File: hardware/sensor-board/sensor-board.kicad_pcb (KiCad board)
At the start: 2 copper layers, 65 x 56 mm, 55 parts, among them J1 HELM, J2 TACH, J3 PROBES, J4 RPi GPIO, U1 ADS1115IDGSR, U2 ADS1115IDGSR, U3 PC817

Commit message: Sensor board rev 1.1: isolated NMEA 2000 on the board
The Fusion stereo (and the depth transducer) now reach the Pi through the
sensor board itself, not a separate CAN HAT:

- MCP2518FD CAN FD controller on SPI0 (GPIO 8-11), interrupt on GPIO 25,
  40 MHz oscillator: Raspberry Pi OS's mcp251xfd overlay makes it can0
- ISO1044 isolated transceiver; the network side is powered from NET-S
  through reverse-polarity, surge and ESD protection and a 5 V regulator,
  referenced to the network's own ground (about 1 LEN)
- J5, a 5-pin locking plug for a drop cable, Micro-C pin order; a 120 ohm
  bench-only terminator behind an open solder jumper
- the network side is its own island: 2 mm from all other copper (DRC rule),
  its own ground pour, kept clear of the Pi mounting hole beside it

The board grows from 65 x 56 to 65 x 76 mm on the side away from the header
(the tach moves down with it, both field plugs on the bottom edge), with a
fifth mounting hole. ERC, DRC and schematic parity all clean.

Also fixes the schematic generator: two symbols derived from one library
parent (SMAJ5.0A, SMAJ18A) shared their unit lists, so renaming one renamed
both and KiCad refused the file; and custom-shaped pads (SOT-89 tab, solder
jumper) are now routed around by their true outline.

Co-Authored-By: Claude Opus 5.5 <noreply@anthropic.com>
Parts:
- added C12: 100n, sensor-board:C_0805_2012Metric_NoSilk, F.Cu at (113.0, 92.2)
- added C13: 1u, sensor-board:C_0805_2012Metric_NoSilk, F.Cu at (113.0, 95.6)
- added C14: 100n, sensor-board:C_0805_2012Metric_NoSilk, F.Cu at (128.5, 92.0)
- added C15: 100n, sensor-board:C_0805_2012Metric_NoSilk, F.Cu at (122.0, 99.8)
- added C16: 1u, sensor-board:C_1206_3216Metric_NoSilk, F.Cu at (117.8, 109.0)
- added C17: 1u, sensor-board:C_0805_2012Metric_NoSilk, F.Cu at (120.3, 109.0)
- added C18: 100n, sensor-board:C_0805_2012Metric_NoSilk, F.Cu at (121.6, 105.2)
- added D10: SMAJ18A, Diode_SMD:D_SMA, F.Cu at (105.5, 112.0)
- added D11: NUP2105L, sensor-board:SOT-23_NoSilk, F.Cu at (125.0, 111.5)
- added D9: SS14, Diode_SMD:D_SMA, F.Cu at (105.5, 108.2)
- added H5: MountingHole, MountingHole:MountingHole_2.7mm_M2.5, F.Cu at (161.5, 122.5)
- added J5: NMEA 2000, Connector_Phoenix_MC:PhoenixContact_MC_1,5_5-GF-3.81_1x05_P3.81mm_Horizontal_ThreadedFlange, F.Cu at (109.0, 117.3)
- added JP1: TERM, Jumper:SolderJumper-2_P1.3mm_Open_RoundedPad1.0x1.5mm, F.Cu at (128.5, 111.8)
- added R26: 120, sensor-board:R_0805_2012Metric_NoSilk, F.Cu at (128.5, 108.0)
- added R27: 10k, sensor-board:R_0805_2012Metric_NoSilk, F.Cu at (132.2, 92.0)
- added R28: 10k, sensor-board:R_0805_2012Metric_NoSilk, F.Cu at (132.2, 96.0)
- added U4: MCP2518FD, Package_SO:SOIC-14_3.9x8.7mm_P1.27mm, F.Cu at (120.5, 94.3)
- added U5: ISO1044BD, Package_SO:SOIC-8_3.9x4.9mm_P1.27mm, F.Cu at (116.5, 102.0)
- added U6: L78L05, Package_TO_SOT_SMD:SOT-89-3, F.Cu at (113.5, 109.0)
- added Y1: 40MHz, Oscillator:Oscillator_SMD_Abracon_ASE-4Pin_3.2x2.5mm, F.Cu at (128.5, 95.5)
- moved C11 20.0 mm to (147.3, 111.5)
- moved D7 20.0 mm to (144.4, 111.5)
- moved J2 20.0 mm to (142.0, 117.3)
- moved R19 20.0 mm to (136.0, 111.5)
- moved R20 20.0 mm to (138.8, 111.5)
- moved R21 20.0 mm to (141.6, 111.5)
- moved U3 20.0 mm to (155.5, 111.5)
- moved R23 18.5 mm to (155.5, 104.3)
- moved R22 16.6 mm to (155.5, 101.8)
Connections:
- J4 pad 19: unconnected-(J4-Pin_19-Pad19) -> /SPI_MOSI
- J4 pad 21: unconnected-(J4-Pin_21-Pad21) -> /SPI_MISO
- J4 pad 22: unconnected-(J4-Pin_22-Pad22) -> /CAN_INT
- J4 pad 23: unconnected-(J4-Pin_23-Pad23) -> /SPI_SCLK
- J4 pad 24: unconnected-(J4-Pin_24-Pad24) -> /SPI_CE0
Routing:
- net +3V3: track 109.6 -> 178.2 mm
- net /CAN_INT: track 0.00 -> 55.5 mm, vias 0 -> 2
- net /SPI_CE0: track 0.00 -> 54.4 mm, vias 0 -> 3
- net /SPI_MISO: track 0.00 -> 42.9 mm, vias 0 -> 2
- net /SPI_SCLK: track 0.00 -> 42.8 mm, vias 0 -> 4
- net /SPI_MOSI: track 0.00 -> 39.6 mm, vias 0 -> 1
- net /N2K_H: track 0.00 -> 26.7 mm, vias 0 -> 2
- net /N2K_GND: track 0.00 -> 23.1 mm, vias 0 -> 2
- net /N2K_L: track 0.00 -> 19.7 mm, vias 0 -> 7
- net /TACH_GPIO: track 33.1 -> 51.0 mm, vias 2 -> 0
- net /N2K_12V: track 0.00 -> 15.7 mm
- net /N2K_5V: track 0.00 -> 12.1 mm, vias 0 -> 4
- net /N2K_NET_S: track 0.00 -> 8.20 mm
- net /CAN_CLK: track 0.00 -> 6.98 mm
- net /N2K_TERM: track 0.00 -> 5.06 mm
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- added copper zone on B.Cu, net /N2K_GND
- added copper zone on F.Cu, net /N2K_GND
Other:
- board size 65 x 56 mm -> 65 x 76 mm
- board text added: "1 SHLD 2 NET-S 3 NET-C"
- board text added: "4 NET-H 5 NET-L"
- board text added: "Boat MFD sensor board r1.1"
- board text added: "J5 NMEA 2000 - ISOLATED"
- board text added: "TERM"
- board text removed: "Boat MFD sensor board r1.0"

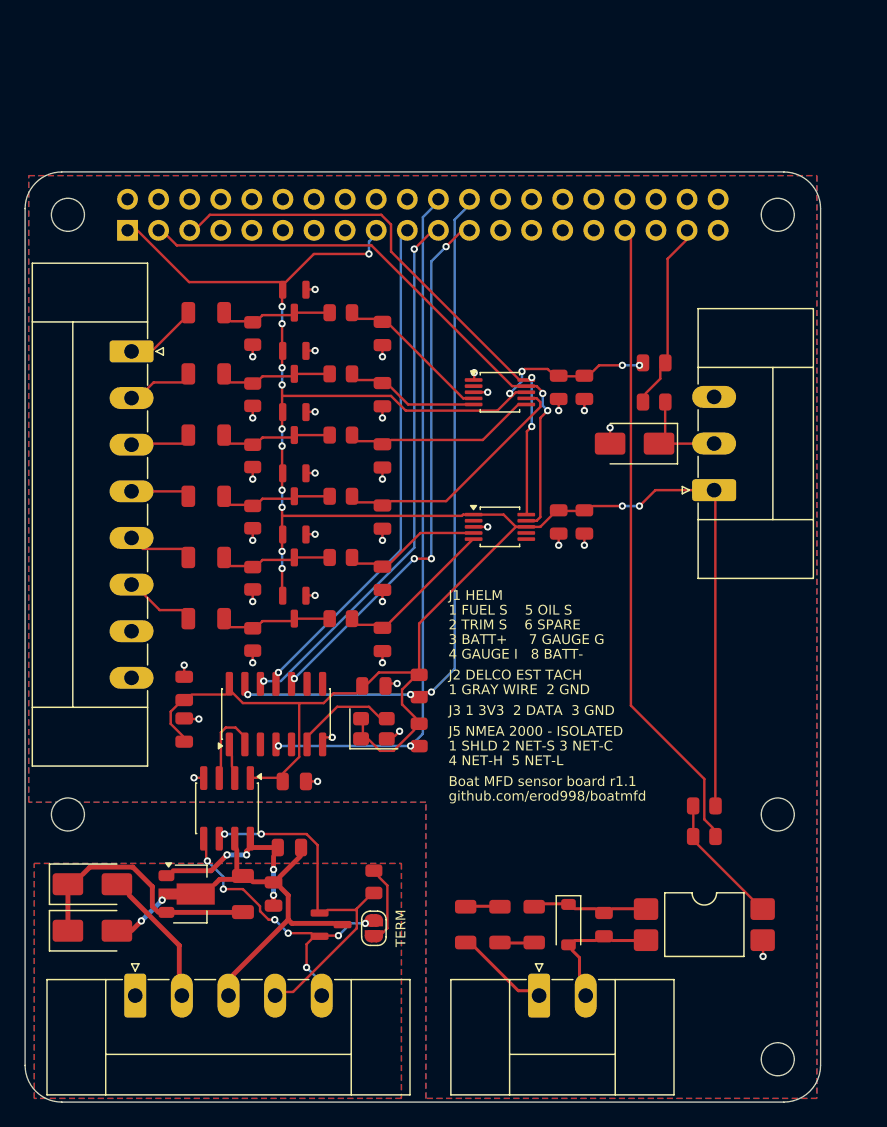
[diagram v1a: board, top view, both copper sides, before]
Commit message: Sensor board: pre-order review and PCBWay order package
Checked against the manufacturers' datasheets rather than KiCad's library:
ISO1044 (TI), MCP2518FD (Microchip Table 1-1), uA78L05 SOT-89 (TI),
NUP2105L (onsemi), EL817 incl. its SMD land pattern (Everlight), Abracon ASE.

Changes from the review:
- U6 is now TI's UA78L05ACPK, whose SOT-89 pinout (1 out, 2 gnd, 3 in) was
  read from TI's datasheet; ST's could not be retrieved to confirm
- C17 1 uF -> 4.7 uF: TI asks for ~4.7 uF bulk at the ISO1044's VCC2
- orderable part numbers for U3 (EL817S1(C)(TU)-F), Y1
  (ASE-40.000MHZ-L-C-T) and every Phoenix header and plug
- vias 0.6 -> 0.7 mm (0.2 mm ring; 0.15 was exactly PCBWay's minimum)
- silkscreen stroke 0.12 -> 0.15 mm (PCBWay's minimum)
- PCBWay's limits written into the design rules so DRC enforces them

fab/pcbway/: Gerbers, BOM and centroid in PCBWay's assembly format, and
ORDER.md with every option for the PCB and assembly quote forms.

Co-Authored-By: Claude Opus 5.5 <noreply@anthropic.com>
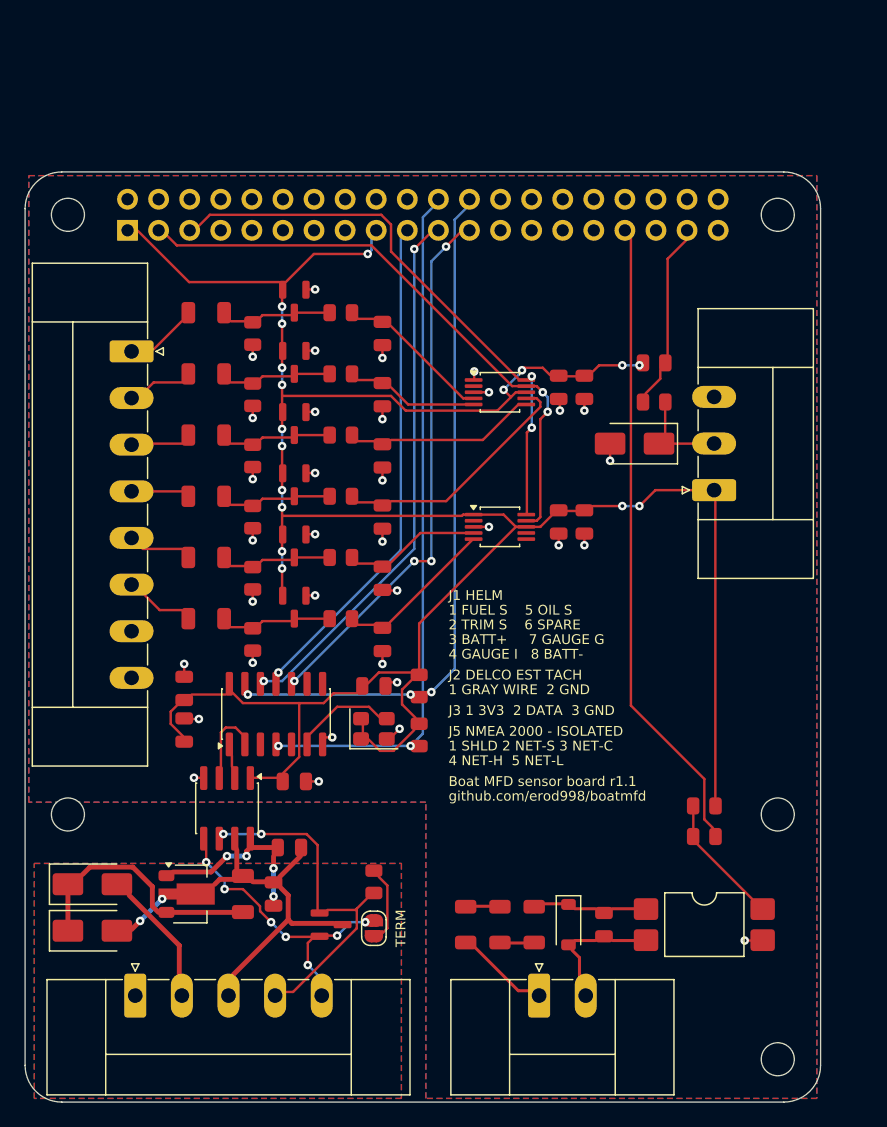
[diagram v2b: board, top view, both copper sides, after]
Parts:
- C17: value 1u -> 4.7u
- U3: value PC817 -> EL817
- U6: value L78L05 -> UA78L05
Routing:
- net GND: track 17.1 -> 18.2 mm
- net +3V3: track 178.2 -> 178.9 mm

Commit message: Sensor board rev 1.2: every connector pin labelled on the board
Each pin of J1, J2, J3 and J5 now has its connection printed beside it, on
the wire side of the connector: FUEL TRIM BAT+ IGN OIL SPARE GND GND on the
helm connector, TACH/GND on the tach, 3V3/DATA/GND on the probes, and the
NMEA 2000 drop cable's wire colours on J5. The numbered pinout block in the
middle is replaced by a WIRING block that says where each kind of wire goes.

Tach wording is for the newer EST coil only (BAT in, TACH out). The input
itself is unchanged: the coil's TACH terminal is its switched side and
spikes to a few hundred volts, which is what the optocoupler input is for.

Parts moved to make room for the labels; the pour is filled after the
board's connectivity is rebuilt, so slivers between the NMEA 2000 pads are
removed instead of left as floating copper. ERC, DRC and parity: clean.

Co-Authored-By: Claude Opus 5.5 <noreply@anthropic.com>
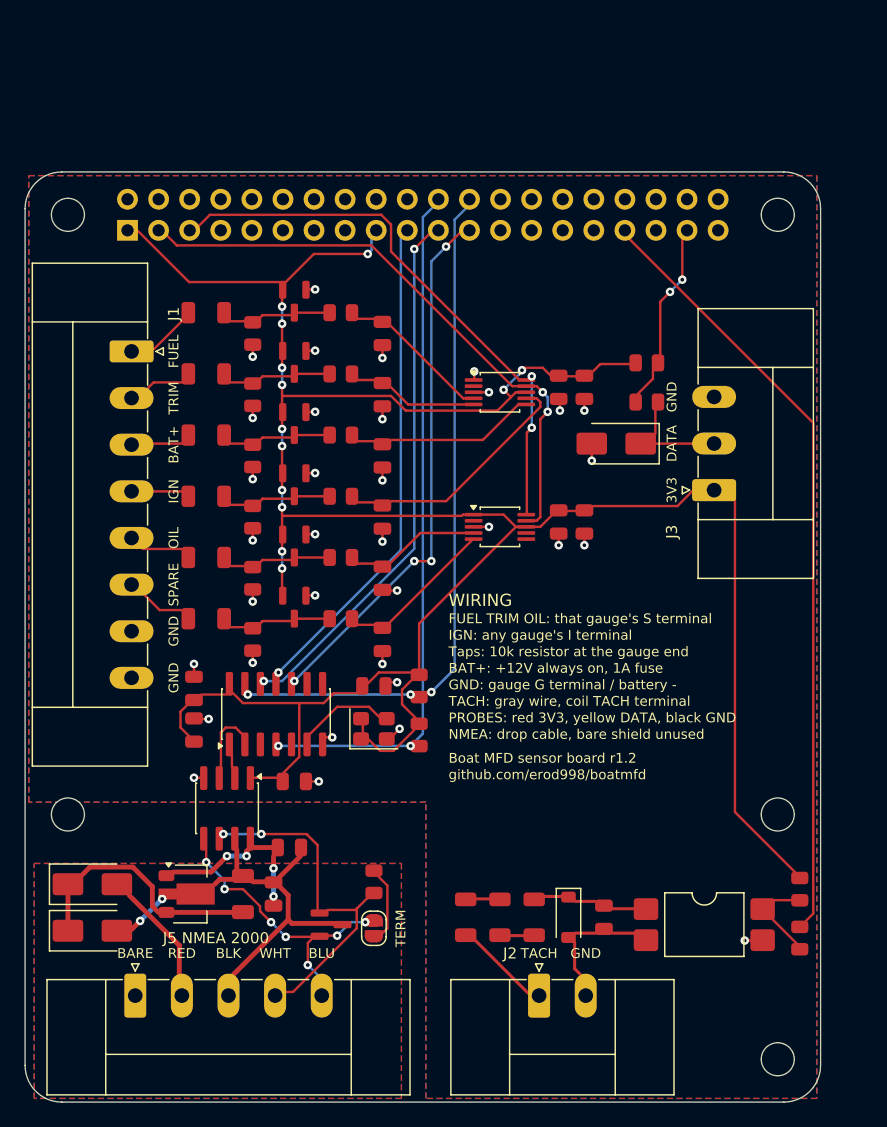
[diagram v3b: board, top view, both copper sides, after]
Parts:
- moved R23 11.4 mm to (163.3, 112.6), turned to 90 degrees
- moved R22 10.3 mm to (163.3, 108.6), turned to 90 degrees
- moved D8 1.50 mm to (148.3, 72.2)
- moved C12 0.80 mm to (113.8, 92.2)
- moved C13 0.80 mm to (113.8, 95.6)
- moved C11 0.60 mm to (147.3, 110.9)
- moved D7 0.60 mm to (144.4, 110.9)
- moved R19 0.60 mm to (136.0, 110.9)
- moved R20 0.60 mm to (138.8, 110.9)
- moved R21 0.60 mm to (141.6, 110.9)
- moved R24 0.60 mm to (150.8, 65.6)
- moved R25 0.60 mm to (150.8, 68.8)
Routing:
- net /TACH_GPIO: track 51.0 -> 62.2 mm
- net +3V3: track 178.9 -> 185.3 mm, vias 17 -> 13
- net /TACH_OUT: track 7.56 -> 4.33 mm
- net /OW_EXT: track 3.60 -> 5.10 mm
- net /TACH_GND: track 5.85 -> 6.41 mm
- net /OW: track 12.3 -> 12.5 mm, vias 0 -> 2
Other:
- board text added: "3V3"
- board text added: "BARE"
- board text added: "BAT+"
- board text added: "BAT+: +12V always on, 1A fuse"
- board text added: "BLK"
- board text added: "BLU"
- board text added: "Boat MFD sensor board r1.2"
- board text added: "DATA"
- board text added: "FUEL"
- board text added: "FUEL TRIM OIL: that gauge's S terminal"
- board text added: "GND"
- board text added: "GND: gauge G terminal / battery -"
- board text added: "IGN"
- board text added: "IGN: any gauge's I terminal"
- board text added: "J1"
- board text added: "J2"
- board text added: "J3"
- board text added: "J5 NMEA 2000"
- board text added: "NMEA: drop cable, bare shield unused"
- board text added: "OIL"
- board text added: "PROBES: red 3V3, yellow DATA, black GND"
- board text added: "RED"
- board text added: "SPARE"
- board text added: "TACH"
- board text added: "TACH: gray wire, coil TACH terminal"
- board text added: "TRIM"
- board text added: "Taps: 10k resistor at the gauge end"
- board text added: "WHT"
- board text added: "WIRING"
- board text removed: "1 FUEL S 5 OIL S"
- board text removed: "1 GRAY WIRE 2 GND"
- board text removed: "1 SHLD 2 NET-S 3 NET-C"
- board text removed: "2 TRIM S 6 SPARE"
- board text removed: "3 BATT+ 7 GAUGE G"
- board text removed: "4 GAUGE I 8 BATT-"
- board text removed: "4 NET-H 5 NET-L"
- board text removed: "Boat MFD sensor board r1.1"
- board text removed: "J1 HELM"
- board text removed: "J2 DELCO EST TACH"
- board text removed: "J3 1 3V3 2 DATA 3 GND"
- board text removed: "J5 NMEA 2000 - ISOLATED"

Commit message: Sensor board: J6 LIGHTS connector for a separate LED board
The LED controllers stay off this board (strip current next to the gauge
taps, and a shorted strip taking the engine data down with it). J6 gives
a future LED board what it needs from the Pi and nothing it switches:
3V3 for its logic, the I2C bus for PCA9685 PWM channels (as many as
needed), GPIO18 and GPIO19 (PWM0/PWM1) for two addressable strips, GPIO21
spare, and two grounds. JST GH 8-way, latching, SMD on the right edge
between the probe connector and the mounting hole; pins labelled on the
silkscreen.

The two lines from the header's far corner route on the bottom layer so
they don't wall off the header's GND pin 39 from the top pour. J6's GND
vias go in before routing. BOM marks J6 SMD (only the Phoenix blocks and
the header are through-hole). SENSOR_BOARD.md documents the interface and
the rules for the LED board; README points to it.

ERC, DRC and parity: clean.

Co-Authored-By: Claude Opus 5.5 <noreply@anthropic.com>
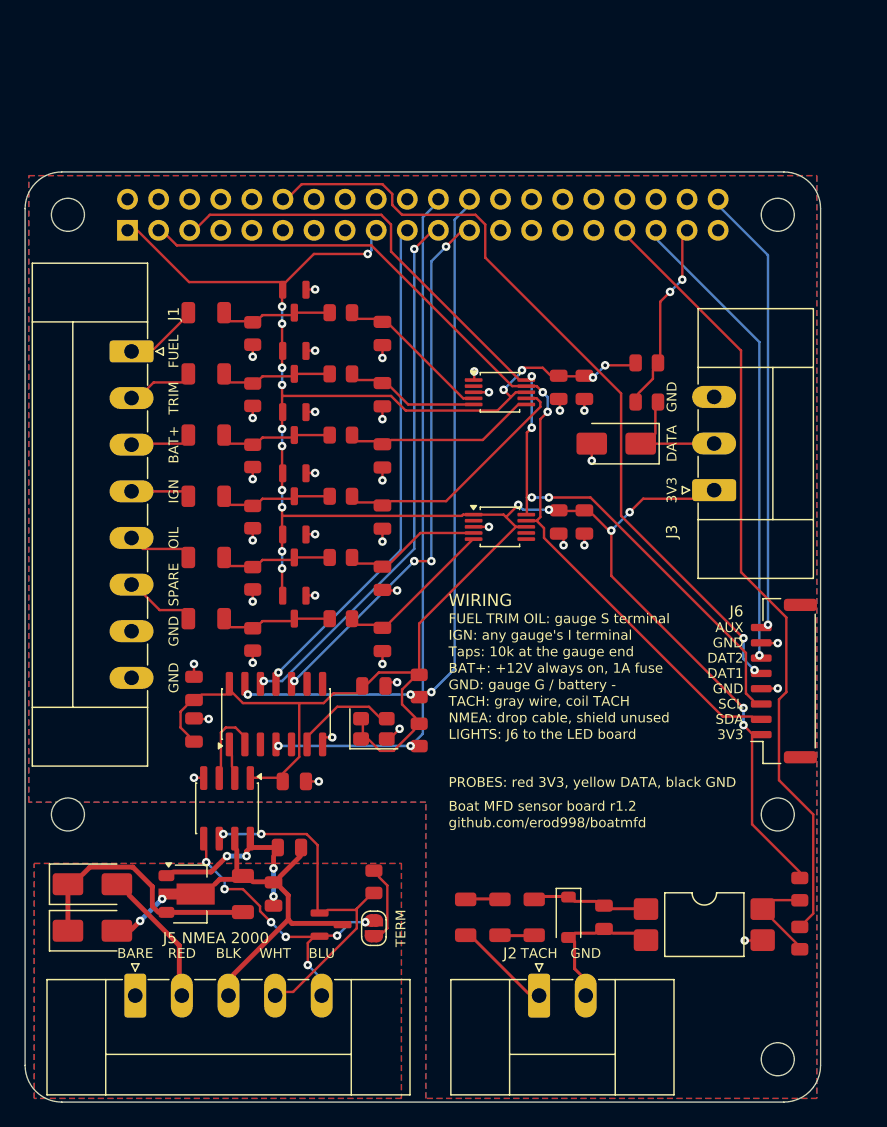
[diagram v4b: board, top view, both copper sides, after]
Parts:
- added J6: LIGHTS, Connector_JST:JST_GH_SM08B-GHS-TB_1x08-1MP_P1.25mm_Horizontal, F.Cu at (162.0, 91.6)
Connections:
- J4 pad 12: unconnected-(J4-Pin_12-Pad12) -> /LIGHT_DAT1
- J4 pad 35: unconnected-(J4-Pin_35-Pad35) -> /LIGHT_DAT2
- J4 pad 40: unconnected-(J4-Pin_40-Pad40) -> /LIGHT_AUX
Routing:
- net /LIGHT_DAT1: track 0.00 -> 63.5 mm, vias 0 -> 2
- net /LIGHT_DAT2: track 0.00 -> 37.3 mm, vias 0 -> 1
- net /LIGHT_AUX: track 0.00 -> 35.6 mm, vias 0 -> 1
- net /SCL: track 44.9 -> 72.2 mm, vias 2 -> 4
- net /SDA: track 45.9 -> 70.6 mm
- net +3V3: track 185.3 -> 190.5 mm, vias 13 -> 21
- net GND: track 18.2 -> 19.2 mm, vias 34 -> 36
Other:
- board text added: "AUX"
- board text added: "DAT1"
- board text added: "DAT2"
- board text added: "FUEL TRIM OIL: gauge S terminal"
- board text added: "GND: gauge G / battery -"
- board text added: "J6"
- board text added: "LIGHTS: J6 to the LED board"
- board text added: "NMEA: drop cable, shield unused"
- board text added: "SCL"
- board text added: "SDA"
- board text added: "TACH: gray wire, coil TACH"
- board text added: "Taps: 10k at the gauge end"
- board text removed: "FUEL TRIM OIL: that gauge's S terminal"
- board text removed: "GND: gauge G terminal / battery -"
- board text removed: "NMEA: drop cable, bare shield unused"
- board text removed: "TACH: gray wire, coil TACH terminal"
- board text removed: "Taps: 10k resistor at the gauge end"

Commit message: Engine temperature from the temp gauge's own sender (J1.6 is now TEMP)
The boat has a temperature gauge with a sender on the engine, so the
board's spare tap becomes TEMP (same circuit; label, net names, docs).

Software (BOAT_TEMP_SENDER=true): the sender is a thermistor, and its
absolute resistance -- which differs between makes, and halves on a
dual-station sender -- folds into the divider fit as the fuel sender's
does. Only the curve's shape matters, and the published curves agree on
it (B about 3900-4000 K). So a cold point (the air or lake temperature
after the engine has sat) and a warm point calibrate the whole gauge,
overheat included: straight lines through the same two points read an
overheat 15-45 F low in simulation; this reads within 5 F even for a
sender at B 3700 K. Three or more widely spread points the published B
can't fit choose their own; points no B fits fall back to straight lines
and say so. A tap wire off is no reading, not boiling.

Coolant source order: a NMEA 2000 converter, then the gauge's sender,
then a clamp-on DS18B20, which fills in with the key off. The probe
offset is refused while the gauge is the source. New Engine temperature
card on /calibrate.

540 tests pass. ERC, DRC and parity: clean.

Co-Authored-By: Claude Opus 5.5 <noreply@anthropic.com>
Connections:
- net /SPARE_ADC renamed /TEMP_ADC
- net /SPARE_DIV renamed /TEMP_DIV
- net /SPARE_IN renamed /TEMP_IN
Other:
- board text added: "FUEL TRIM OIL TEMP: S terminal"
- board text added: "TEMP"
- board text removed: "FUEL TRIM OIL: gauge S terminal"
- board text removed: "SPARE"
